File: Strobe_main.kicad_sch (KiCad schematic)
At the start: 0 parts

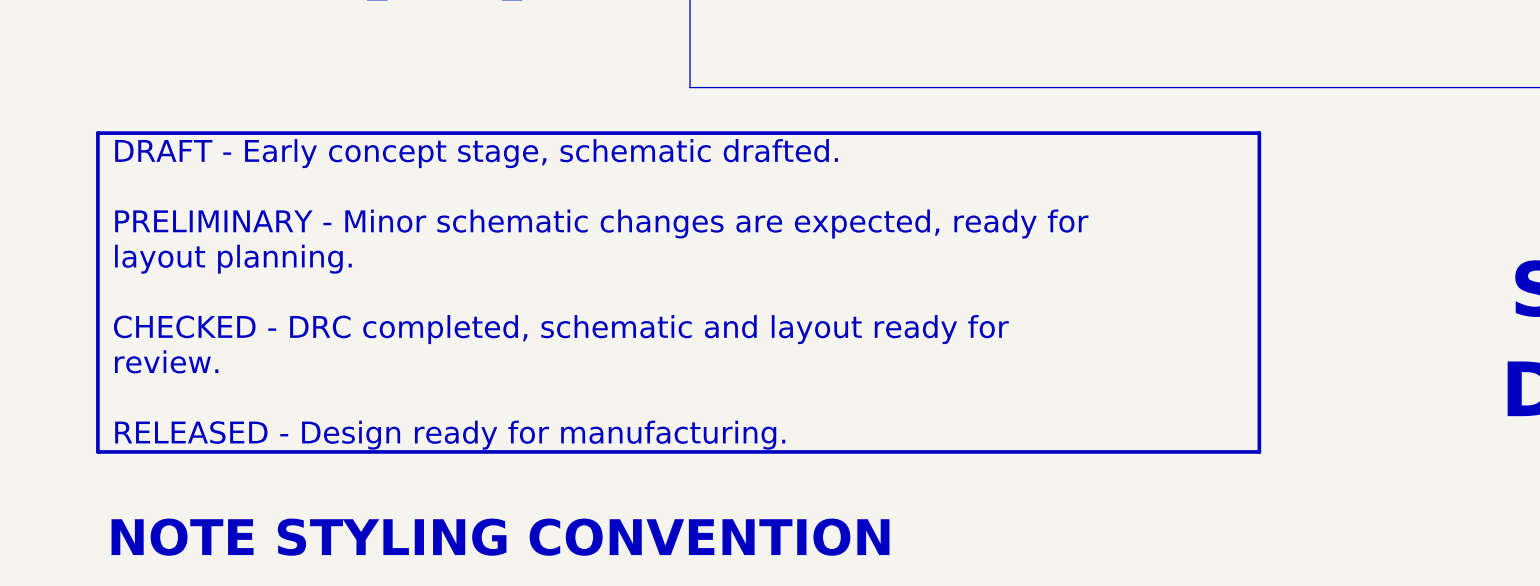
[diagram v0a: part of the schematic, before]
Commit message: Reworked sheet titles
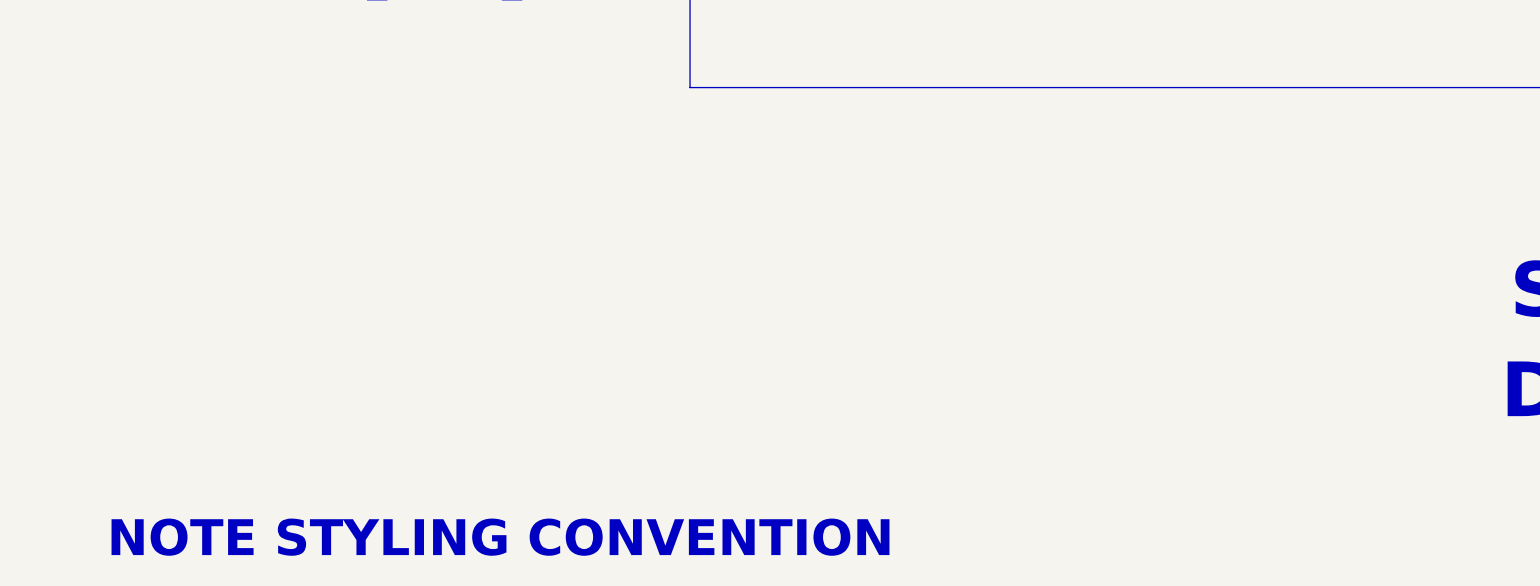
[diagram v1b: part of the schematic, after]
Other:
- title: (none) -> ${SHEETNAME}
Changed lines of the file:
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@@
 	(paper "A3")
 	(title_block
+		(title "${SHEETNAME}")
 		(date "2025-01-12")
 		(rev "${REVISION}")
@@
 		)
 	)
-	(text_box "DRAFT - Early concept stage, schematic drafted.\n\nPRELIMINARY - Minor schematic changes are expected, ready for layout planning.\n\nCHECKED - DRC completed, schematic and layout ready for review.\n\nRELEASED - Design ready for manufacturing."
-		(exclude_from_sim no)
-		(at 25.4 196.85 0)
-		(size 161.925 44.45)
-		(margins 2 2 2 2)
-		(stroke
-			(width 0.508)
-			(type solid)
-			(color 132 132 132 1)
-		)
-		(fill
-			(type color)
-			(color 200 200 200 1)
-		)
-		(effects
-			(font
-				(face "Arial")
-				(size 3.048 3.048)
-				(color 0 0 0 1)
-			)
-			(justify left)
-		)
-	)
